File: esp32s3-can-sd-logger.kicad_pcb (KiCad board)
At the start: 4 copper layers, 84 x 74 mm, 168 parts, among them J1 PWR + CAN harness, J10 Sensor harness, J2 USB-C, J3 UART0, J4 I2C / Qwiic, J5 SPI, J6 WS2812, J7 Spare IO, J8 Rail break-out, J9 microSD push-pull, Q1 100V 6.8mOhm N-ch, Q2 -20V 2.3A P-ch, Q3 60V 300mA N-ch, SW1 RESET, SW2 BOOT, U1 LM74700-Q1, U2 LM5164 (5V), U3 LM5164 (3V3), U4 ESP32-S3-WROOM-1-N16R8, U5 USBLC6-2SC6, U6 74AHCT1G125, U7 TJA1051T/3, U8 ADS1115

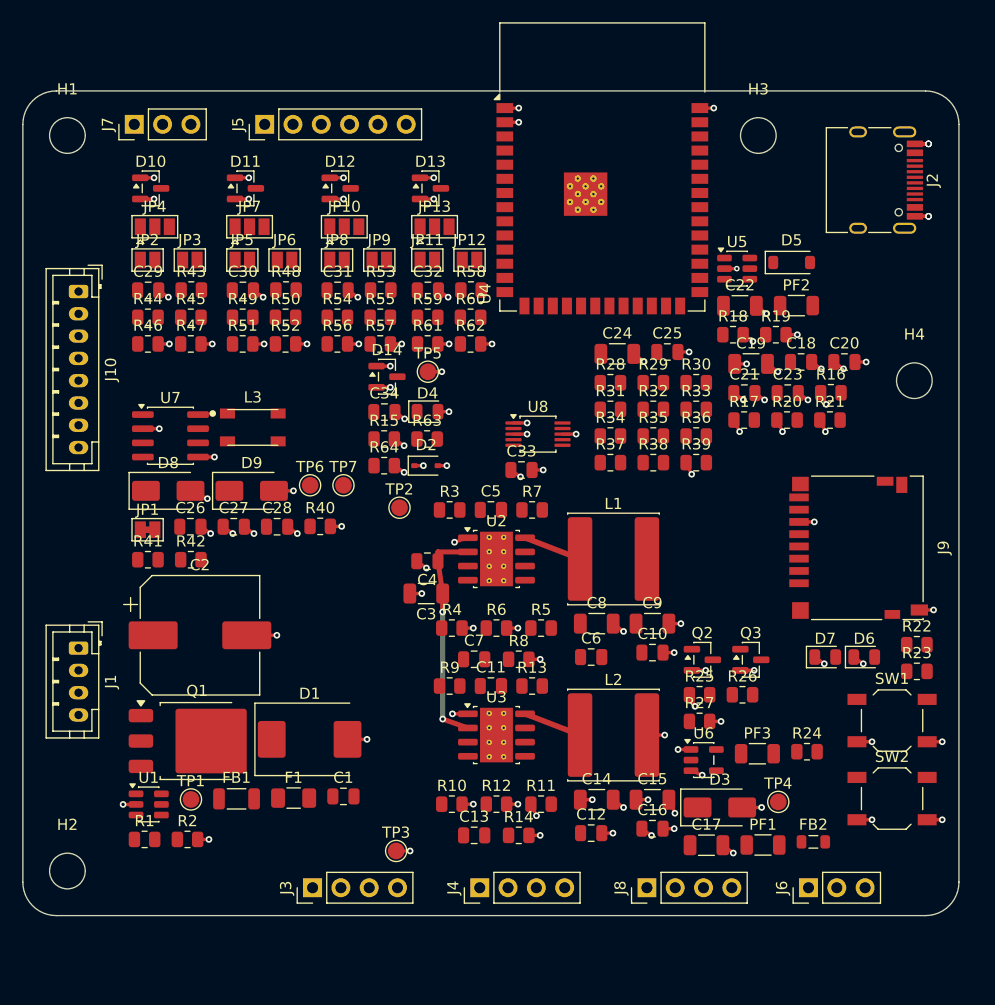
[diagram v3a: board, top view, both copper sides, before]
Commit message: Route the board: 338 of 341 connections, DRC-clean
The board now carries ~1500 tracks and 210 vias over solid GND and +3V3
planes, and kicad-cli pcb drc reports zero violations. Three connections
in the two most congested blocks are left for the interactive router and
are named in README section 10.

What made routing work, beyond the plane-safe DSN and pre-stitched plane
vias added in the previous commit:

- Per-zone part spacing. The microSD block is nothing but series
  resistors that all have to be routed through, and at the global 0.4 mm
  courtyard gap there was no channel for a 0.2 mm track with clearance
  either side, so the router could not get in at all. That one zone now
  packs at 0.85 mm. Raising the gap everywhere was tried and made things
  much worse (33 violations), so it stays local.
- Deduplicating vias on stacked pads. A connector's duplicated pins
  (USB-C A1/B12 share coordinates) were each getting their own via at the
  same spot, and freerouting hung on the resulting overlap -- twice, for
  ten minutes each, before the log gave it away.
- A gap-closing pass in finish_routing.py that routes the short leftovers
  DRC reports, trying a straight segment then an L on either side, on
  F.Cu then B.Cu, all checked against real pad and track geometry.

fab/ now holds the JLCPCB package: Gerbers + drill zipped, bom.csv and
positions.csv in JLC's column layout. Gerber output is gitignored since
it regenerates from the board.

Co-Authored-By: Claude Fable 5 <noreply@anthropic.com>
Claude-Session: https://claude.ai/code/session_01DhNbL25h25p8VFCjRfJik9
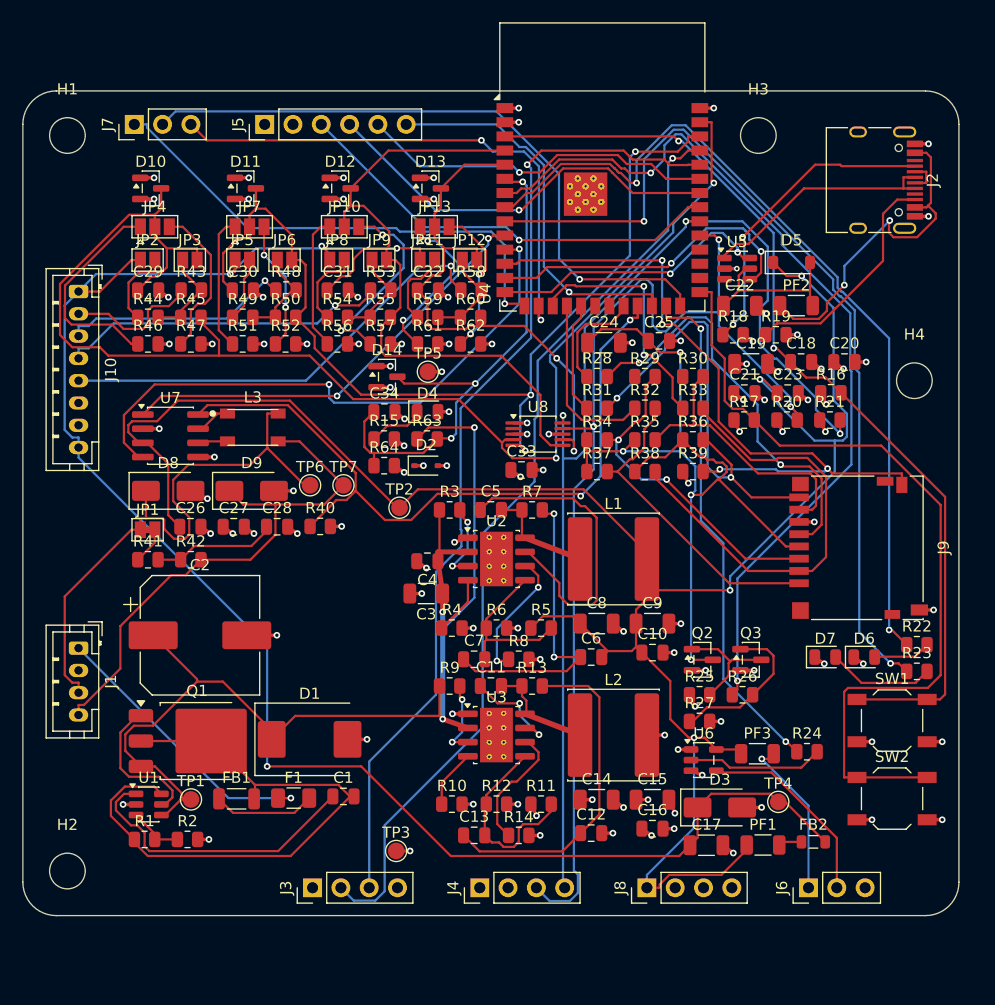
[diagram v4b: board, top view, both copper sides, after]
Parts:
- moved C24 1.56 mm to (52.1, 22.6)
- moved R37 1.44 mm to (51.5, 34.2)
- moved R28 1.32 mm to (51.5, 25.6)
- moved R34 1.25 mm to (51.5, 31.3)
- moved C25 1.25 mm to (57.1, 22.4)
- moved R31 1.20 mm to (51.5, 28.5)
- moved R38 1.10 mm to (55.8, 34.2)
- moved R29 0.93 mm to (55.8, 25.6)
- moved R39 0.85 mm to (60.1, 34.2)
- moved R35 0.83 mm to (55.8, 31.3)
- moved R32 0.76 mm to (55.8, 28.5)
- moved R30 0.63 mm to (60.1, 25.6)
- moved R36 0.46 mm to (60.1, 31.3)
- moved R33 0.32 mm to (60.1, 28.5)
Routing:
- net +5V: track 0.00 -> 184.9 mm, vias 0 -> 4
- net +5VS: track 0.00 -> 153.4 mm, vias 0 -> 4
- net AIN1: track 0.00 -> 123.0 mm, vias 0 -> 2
- net I2C_SCL: track 0.00 -> 100.6 mm, vias 0 -> 3
- net I2C_SDA: track 0.00 -> 97.8 mm, vias 0 -> 3
- net AIN2: track 0.00 -> 88.0 mm, vias 0 -> 3
- net UART_RX: track 0.00 -> 87.7 mm, vias 0 -> 1
- net MCU_EN: track 0.00 -> 84.8 mm, vias 0 -> 2
- net UART_TX: track 0.00 -> 84.0 mm, vias 0 -> 1
- net +VBAT: track 20.1 -> 103.0 mm, vias 2 -> 3
- net SD_PWR_EN: track 0.00 -> 80.8 mm, vias 0 -> 2
- net LED2: track 0.00 -> 80.1 mm, vias 0 -> 2
- net SD_VDD: track 0.00 -> 77.2 mm, vias 0 -> 4
- net LED1: track 0.00 -> 76.9 mm, vias 0 -> 2
- net MCU_BOOT: track 0.00 -> 74.2 mm
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
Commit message: Finish the board: rip-up routing closes the last three connections
The autorouter left SD_CMD, SD_D0 and USB_DM_CON open, and no amount of
searching was going to find them a path -- there wasn't one. It routes the
easy nets first and fences the awkward ones in: SD_CLK ran straight under
the ESP32 module's pads 20 and 21 and walled both off, and at 1.27 mm pitch
nothing slips past sideways.

gen/maze_route.py does what a person does. It grids each copper layer at
0.1 mm from real pad, track, via and keepout geometry, searches both layers
at once with Dijkstra, and when that fails works out which nets are pressed
against the dead end, tears them out, routes the trapped net through the
space they leave, and re-routes them on a later pass.

Three details decide whether that converges or thrashes:

  - A rip removes tracks, never pads. Letting a ripped net's pads vanish
    too had it laying copper straight across them.
  - Blockers are ranked from the tighter pocket. Flooding from both ends
    and scoring both, an end with the run of the board contributes a
    frontier thousands of cells long and the bystanders along it drown out
    the few nets actually doing the trapping.
  - A connection is to a net, not a pad. USB-C carries D- on both A7 and
    B7; A7 escapes only down a 16 um corridor, finer than any grid, while
    B7 opens onto the whole board. Aiming at the net's existing copper
    turned an impossible route into an easy one.

Nets with more than four pads are never ripped -- a two-pad signal comes
back as one trace, a rail daisy-chaining six caps comes back as six
connections that can each fail. Every path is re-checked against the grid
before it becomes copper, so a planning-and-reality mismatch surfaces as a
refusal rather than as DRC errors afterwards.

341 of 341 connections routed, zero DRC errors, zero unconnected:
1340 tracks, 222 vias.

gen/tidy_silk.py then hides the value fields, drops references to 0.8 mm
(the floor for both the board's text rul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
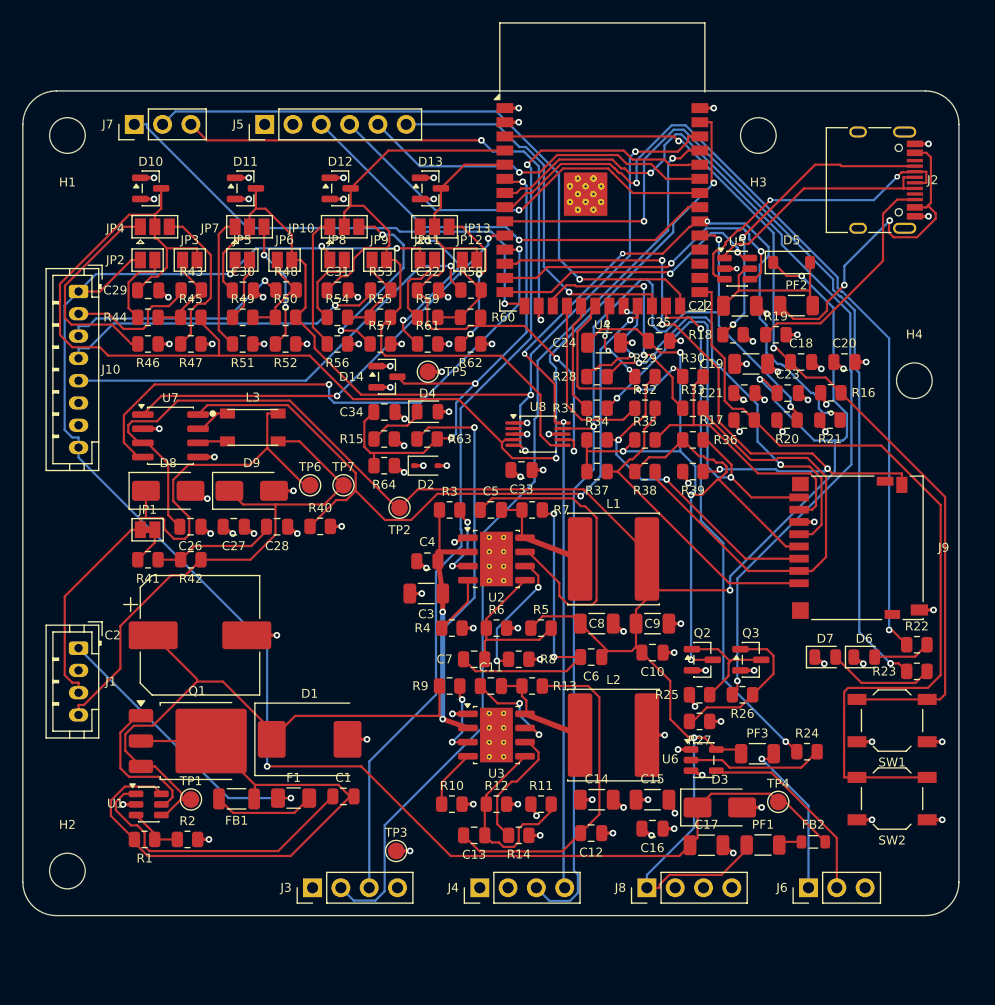
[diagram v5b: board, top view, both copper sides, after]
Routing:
- net USB_DM_CON: track 3.05 -> 25.9 mm, vias 0 -> 2
- net SD_D0: track 0.00 -> 16.9 mm, vias 0 -> 2
- net I2C_SCL: track 100.6 -> 93.6 mm, vias 3 -> 5
- net SD_CMD: track 0.00 -> 6.11 mm, vias 0 -> 4
- net SD_CLK: track 9.66 -> 9.37 mm, vias 0 -> 2

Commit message: Fix netclasses being silently lost: the power rails were 0.2 mm
Checking the ESP32 pin assignments turned up something worse than a pin
conflict. The committed project file held only the Default netclass and
zero netclass patterns, so Power (0.5 mm track, 0.8 mm via) and CAN had
never been applied and the whole board routed at 0.2 mm -- including +5V
and +5VS, which are 1 A rails.

Nothing caught it because narrow track is legal track. 0.2 mm in 1 oz
copper is 1.01 A at a 20 C rise and drops 147 mV over a 60 mm run; on
+5VS, the sensor excitation rail, that droop lands straight on every
ratiometric reading the 0.1% dividers and the 16-bit ADC exist to
protect.

Three separate causes, all fixed:

  - generate_pcb.py builds its board with CreateEmptyBoard(), which knows
    only the Default class, and saving it rewrote the .kicad_pro from the
    board's own settings. It now lifts net_settings out before the save
    and restores it after, and says what it restored.

  - maze_route.py and finish_routing.py hardcoded 0.2 mm for their
    fix-up traces, so +5VS came back 58 mm at the correct 0.5 mm and
    89 mm at 0.2. Both now size tracks and vias per net through the new
    gen/netclasses.py, which reads the classes and their glob patterns
    from the project file -- net.GetNetClass() hands back an undecorated
    SwigPyObject here, and a try/except around it is exactly how a
    default silently becomes a power rail.

  - The min-drill rule (0.2 mm, needed by the LM5164 thermal vias) lived
    only in the board object, so regenerating the schematic reset it to
    0.3 and made those vias illegal. It is in the project template now,
    so it survives in either order.

Also fixed, found while re-routing: the island builder rasterised pads
from their bounding boxes, but a 1.70 mm round header pad's bounding box
corners are ~0.35 mm off the copper, so 23% of the apparent landing area
is bare laminate. Routes ended there, connected nothing, and the router
then called th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
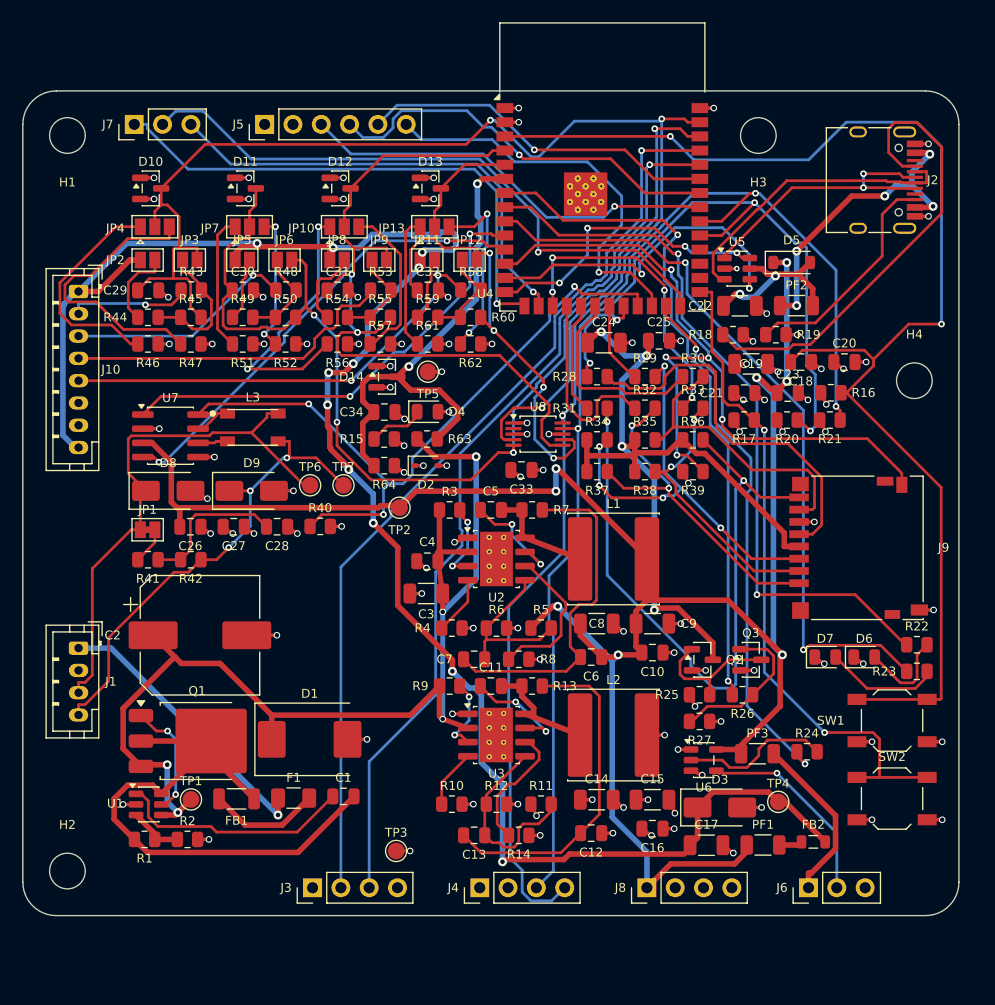
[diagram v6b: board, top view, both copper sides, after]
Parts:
- R34, R35, R36, R37, R38: value 47k -> 10k
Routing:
- net MCU_EN: track 84.8 -> 117.0 mm
- net SD_D1_C: track 39.2 -> 60.5 mm
- net SD_PWR_EN: track 80.8 -> 61.4 mm
- net BST_5V: track 28.2 -> 9.87 mm, vias 0 -> 2
- net I2C_SCL: track 93.6 -> 111.3 mm, vias 5 -> 3
- net SD_D3_C: track 41.0 -> 24.5 mm, vias 0 -> 2
- net USB_CC1: track 27.8 -> 42.1 mm, vias 2 -> 0
- net MCU_BOOT: track 74.2 -> 60.3 mm, vias 0 -> 2
- net LED2: track 80.1 -> 67.3 mm
- net AIN3_R1: track 12.2 -> 24.6 mm, vias 0 -> 2
- net AIN2: track 88.0 -> 100.2 mm, vias 3 -> 4
- net AIN1_R2: track 14.3 -> 25.4 mm
- net CAN_RX: track 52.6 -> 41.8 mm
- net LED1: track 76.9 -> 66.1 mm
- net +5VS: track 153.4 -> 163.4 mm, vias 4 -> 11
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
